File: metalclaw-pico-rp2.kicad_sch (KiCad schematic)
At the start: 123 parts, among them J1 USB4105-GF-A, J2 FTSH-105-01-L-DV-K, SW1 PTS810SJM250SMTR LFS, SW2 PTS810SJM250SMTR LFS, U1 XC6220B331MR-G, U2 RP2354B, U3 APS6404L-3SQR-SN, Y1 ABM8-272-T3

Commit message: Route USB, PSRAM and first quadrant signals
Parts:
- D1: value PMEG2010ER,115 -> CUHS20F30,H3F; footprint Diode_SMD:Nexperia_CFP3_SOD-123W -> Diode_SMD:D_SOD-323F; Mouser 771-PMEG2010ER115 -> 757-CUHS20F30H3F
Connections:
- net USB_D-: now reaches R80.2, U2.66 (USB_DM)
- net USB_D+: now reaches R81.2, U2.67 (USB_DP)
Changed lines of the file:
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@@
 		)
 	)
+	(label "USB_D+"
+		(at 330.2 123.19 180)
+		(effects
+			(font
+				(size 1.27 1.27)
+			)
+			(justify right bottom)
+		)
+	)
 	(label "GP7"
 		(at 43.18 172.72 0)
@@
 		)
 	)
+	(label "USB_D-"
+		(at 330.2 120.65 180)
+		(effects
+			(font
+				(size 1.27 1.27)
+			)
+			(justify right bottom)
+		)
+	)
 	(label "GP26"
 		(at 191.77 182.88 180)
@@
 			)
 		)
-		(property "Value" "PMEG2010ER,115"
+		(property "Value" "CUHS20F30,H3F"
 			(at 343.8525 69.85 0)
 			(effects
@@
 			)
 		)
-		(property "Footprint" "Diode_SMD:Nexperia_CFP3_SOD-123W"
+		(property "Footprint" "Diode_SMD:D_SOD-323F"
 			(at 344.17 73.66 0)
 			(effects
@@
 			)
 		)
-		(property "Datasheet" "https://assets.nexperia.com/documents/data-sheet/PMEG2010ER.pdf"
+		(property "Datasheet" "https://toshiba.semicon-storage.com/info/CUHS20F30_datasheet_en_20250926.pdf?did=63604&prodName=CUHS20F30"
 			(at 344.17 73.66 0)
 			(effects
@@
 			)
 		)
-		(property "Description" "20 V 1 A low-forward-voltage Schottky rectifier, SOD-123W, Nexperia PMEG2010ER,115"
+		(property "Description" "30 V 2 A Schottky barrier diode, SOD-323HE (US2H), Toshiba CUHS20F30,H3F"
 			(at 344.17 73.66 0)
 			(effects
@@
 			)
 		)
-		(property "Mouser" "771-PMEG2010ER115"
+		(property "Mouser" "757-CUHS20F30H3F"
 			(at 344.17 73.66 0)
 			(effects

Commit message: Route all signals
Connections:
- net USB_D+: now also J1.A6 (D+), J1.B6 (D+), R81.1; no longer R81.2, U2.67 (USB_DP)
- net USB_D-: now also J1.A7 (D-), J1.B7 (D-), R80.1; no longer R80.2, U2.66 (USB_DM)
- new net: R80.2, U2.66 (USB_DM)
- new net: R81.2, U2.67 (USB_DP)
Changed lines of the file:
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@@
 	)
 	(label "USB_D+"
-		(at 330.2 123.19 180)
+		(at 347.98 123.19 180)
 		(effects
 			(font
@@
 	)
 	(label "USB_D-"
-		(at 330.2 120.65 180)
-		(effects
-			(font
+		(at 347.98 120.65 180)
+		(effects
+			(font

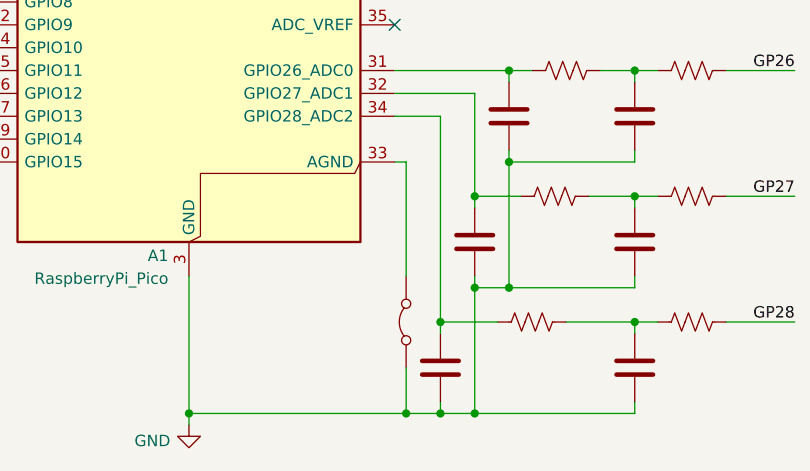
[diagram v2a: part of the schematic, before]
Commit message: Rearrange power passives
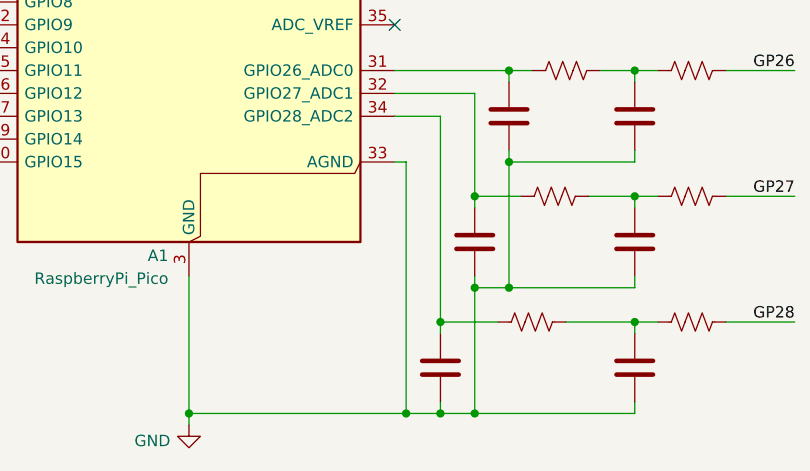
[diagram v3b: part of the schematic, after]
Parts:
- removed JP1: Jumper_2_Bridged, Jumper:SolderJumper-2_P1.3mm_Bridged2Bar_Pad1.0x1.5mm, symbol Jumper:Jumper_2_Bridged
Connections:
- net GND: now also A1.33 (AGND)
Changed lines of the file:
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@@
 	(wire
 		(pts
-			(xy 148.59 215.9) (xy 148.59 220.98)
+			(xy 148.59 193.04) (xy 148.59 220.98)
 		)
 		(stroke
@@
 	(wire
 		(pts
-			(xy 148.59 193.04) (xy 148.59 205.74)
-		)
-		(stroke
-			(width 0)
-			(type default)
-		)
-	)
-	(wire
-		(pts
 			(xy 257.81 105.41) (xy 245.11 105.41)
 		)
@@
 					(unit 1)
 				)
-			)
-		)
-	)
-	(symbol
-		(lib_id "Jumper:Jumper_2_Bridged")
-		(at 148.59 210.82 90)
-		(unit 1)
-		(exclude_from_sim no)
-		(in_bom no)
-		(on_board yes)
-		(dnp no)
-		(property "Reference" "JP1"
-			(at 146.05 209.5499 90)
-			(effects
-				(font
-					(size 1.27 1.27)
-				)
-				(justify left)
-				(hide yes)
-			)
-		)
-		(property "Value" "Jumper_2_Bridged"
-			(at 146.05 212.0899 90)
-			(effects
-				(font
-					(size 1.27 1.27)
-				)
-				(justify left)
-				(hide yes)
-			)
-		)
-		(property "Footprint" "Jumper:SolderJumper-2_P1.3mm_Bridged2Bar_Pad1.0x1.5mm"
-			(at 148.59 210.82 0)
-			(effects
-				(font
-					(size 1.27 1.27)
-				)
-				(hide yes)
-			)
-		)
-		(property "Datasheet" "~"
-			(at 148.59 210.82 0)
-			(effects
-				(font
-					(size 1.27 1.27)
-				)
-				(hide yes)
-			)
-		)
-		(property "Description" "Jumper, 2-pole, closed/bridged"
-			(at 148.59 210.82 0)
-			(effects
-				(font
-					(size 1.27 1.27)
-				)
-				(hide yes)
-			)
-		)
-		(property "KLC_S4.2_DVDD" ""
-			(at 148.59 210.82 90)
-			(effects
-				(font
-					(size 1.27 1.27)
-				)
-				(hide yes)
-			)
-		)
-		(property "KLC_S4.2_VREG_LX" ""
-			(at 148.59 210.82 90)
-			(effects
-				(font
-					(size 1.27 1.27)
-				)
-				(hide yes)
-			)
-		)
-		(pin "1"
-		)
-		(pin "2"
-		)
-		(instances
-			(project ""
-				(path "/c83ebc88-59c8-491c-acdb-d3cfac2d55f0"
-					(reference "JP1")
-					(unit 1)
-				)

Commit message: Castellate A1 edge pads, fix D1 footprint (US2H), GND stitching, DRC clean
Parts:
- D1: footprint Diode_SMD:D_SOD-323F -> MetalClaw:D_US2H_CUHS20F30
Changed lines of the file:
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@@
 			)
 		)
-		(property "Footprint" "Diode_SMD:D_SOD-323F"
+		(property "Footprint" "MetalClaw:D_US2H_CUHS20F30"
 			(at 344.17 73.66 0)
 			(effects

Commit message: BOM: R83 CE pull-up 10k->2.2k, LCSC part numbers, L1 entry fix
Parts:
- C1, C2: LCSC (none) -> C19702; LCSC MPN (none) -> CL10A106KP8NNNC
- C10, C12, C13, C24: LCSC (none) -> C326586; LCSC MPN (none) -> CC0402KRX5R6BB475
- C11, C28: LCSC (none) -> C52923; LCSC MPN (none) -> CL05A105KA5NQNC
- C14, C15, C16, C17, C18, C19, C20, C21, C22, C23, C25, C3: LCSC (none) -> C190183; LCSC MPN (none) -> CC0201KRX5R6BB104
- C26, C27: LCSC (none) -> C85891
- C4, C5, C6: LCSC (none) -> C668348
- C7, C8, C9: LCSC (none) -> C326875; LCSC MPN (none) -> CC0201KRX7R8BB103
- D1: LCSC (none) -> C5357828
- J1: LCSC (none) -> C3020560
- J2: LCSC (none) -> C5155080
- L1: LCSC (none) -> C42411119
- R1, R10, R11, R12, R13, R14, R15, R16, R17, R19, R2, R20, R21, R22, R25, R27, R28, R29, R3, R4, R5, R6, R7, R79, R8, R82, R9: LCSC (none) -> C274341
- R18, R34, R42, R78: LCSC (none) -> C138165
- R23, R24, R26: LCSC (none) -> C142018
- R30, R31, R32: LCSC (none) -> C274872
- R33, R35, R36, R37, R38, R39, R40, R41, R43, R44, R45, R46, R47, R48, R49, R50, R51, R52, R53, R54, R55, R56, R57, R58, R59, R60, R61, R62, R63, R64, R65, R66, R67, R68, R69, R70, R71, R72, R74, R75, R76, R77: LCSC (none) -> C77623
- R73: LCSC (none) -> C25105; LCSC MPN (none) -> 0402WGF330JTCE
- R80, R81: LCSC (none) -> C273268
- R83: value 10k -> 2.2k; LCSC (none) -> C142018; Mouser 603-RC0201FR-0710KL -> 603-RC0201FR-072K2L
- SW1, SW2: LCSC (none) -> C116501
- U1: LCSC (none) -> C86534
- U2: LCSC (none) -> C39843328
- U3: LCSC (none) -> C5333729
- Y1: LCSC (none) -> C20625731

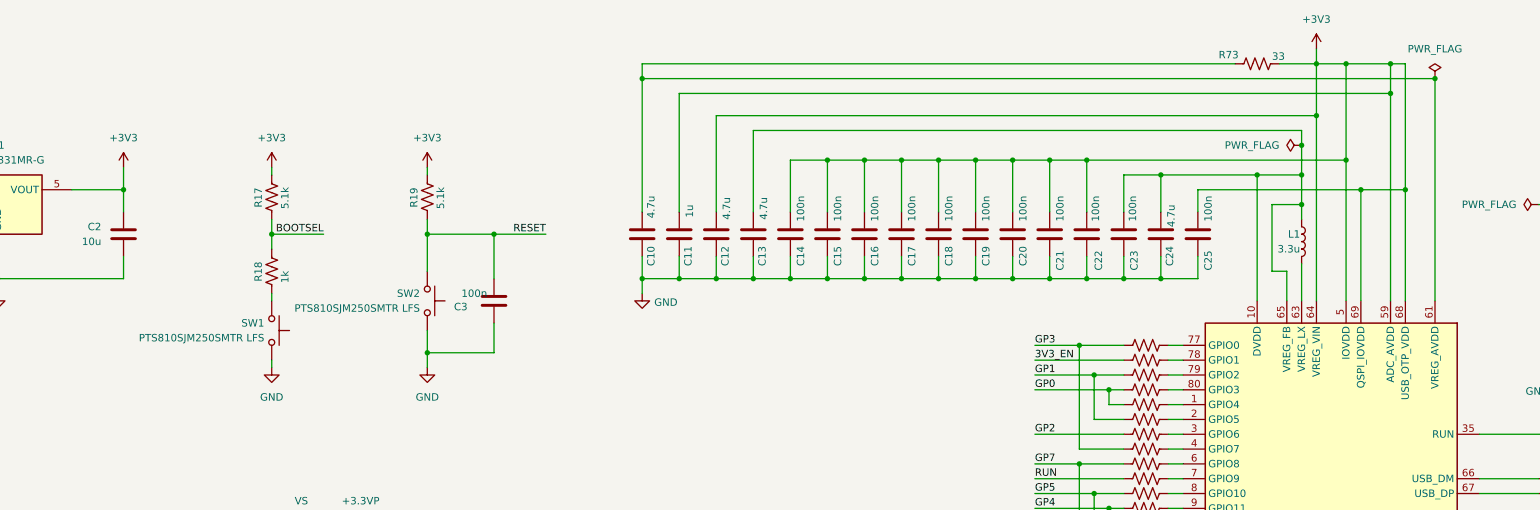
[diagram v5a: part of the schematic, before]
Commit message: Add decoupling for pin 51
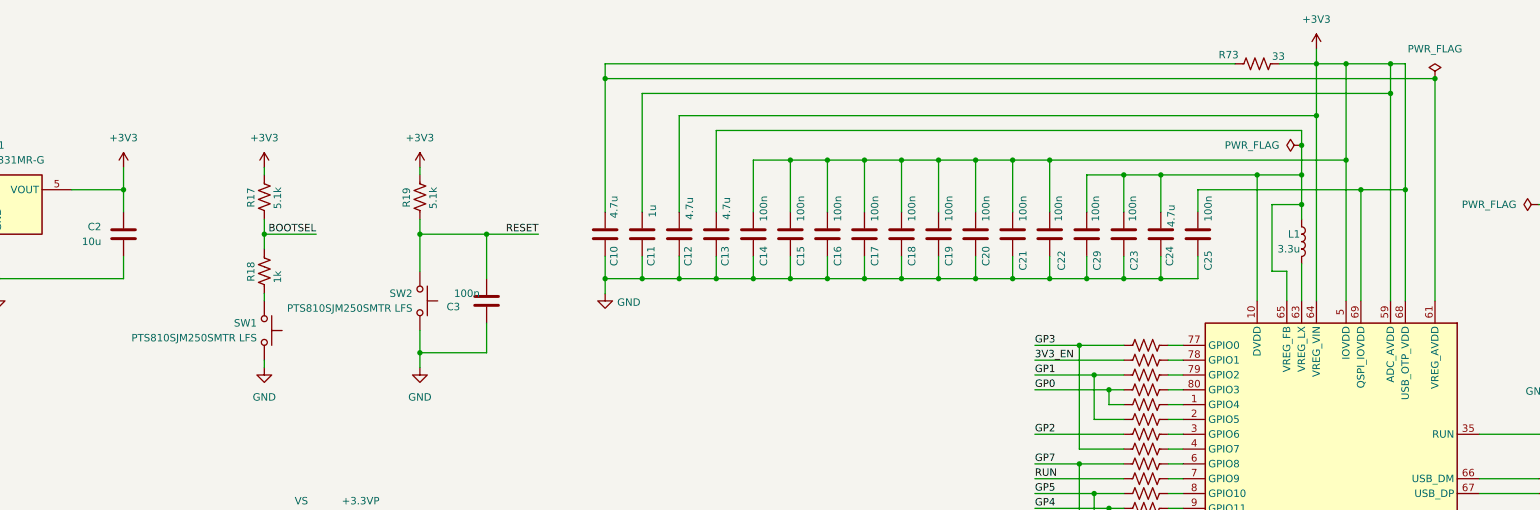
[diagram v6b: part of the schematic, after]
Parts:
- added C29: 100n, Capacitor_SMD:C_0201_0603Metric, symbol Device:C
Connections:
- net GND: now also C29.1
- net at C13.2, C23.2, C24.2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: now also C29.2
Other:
- moved on the sheet: C10, C11, C12, C13, C14, C15, C16, C17, C18, C19, C20, C21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

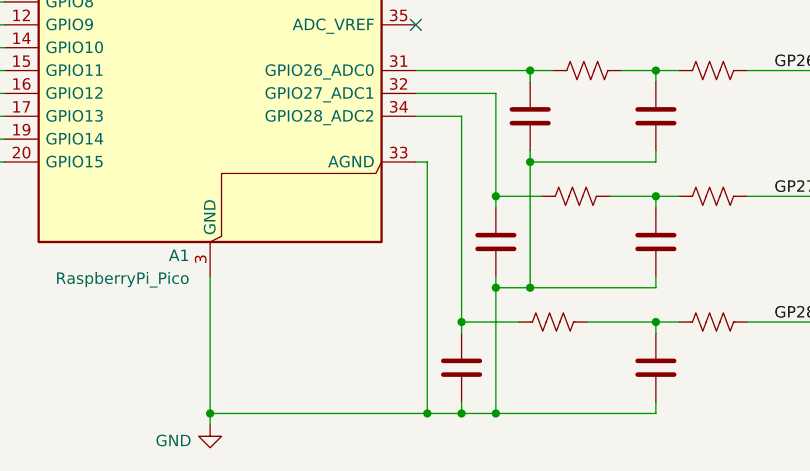
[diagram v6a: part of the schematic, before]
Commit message: Use net tie to connect AGND and GND
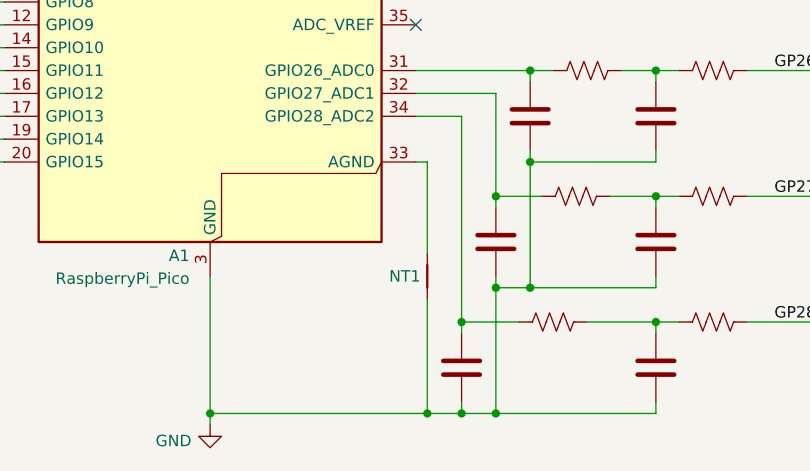
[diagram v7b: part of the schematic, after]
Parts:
- added NT1: NetTie_2, NetTie:NetTie-2_SMD_Pad0.5mm, symbol Device:NetTie_2
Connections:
- net GND: now also NT1.1; no longer A1.33 (AGND)
- new net: A1.33 (AGND), NT1.2
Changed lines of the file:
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@@
 	)
 	(junction
+		(at 148.59 220.98)
+		(diameter 0)
+		(color 0 0 0 0)
+	)
+	(junction
 		(at 171.45 86.36)
 		(diameter 0)
@@
 	)
 	(junction
-		(at 148.59 220.98)
-		(diameter 0)
-		(color 0 0 0 0)
-	)
-	(junction
 		(at 364.49 193.04)
 		(diameter 0)
@@
 	(wire
 		(pts
-			(xy 148.59 193.04) (xy 148.59 220.98)
-		)
-		(stroke
-			(width 0)
-			(type default)
-		)
-	)
-	(wire
-		(pts
 			(xy 124.46 220.98) (xy 124.46 222.25)
 		)
@@
 	(wire
 		(pts
+			(xy 148.59 208.28) (xy 148.59 220.98)
+		)
+		(stroke
+			(width 0)
+			(type default)
+		)
+	)
+	(wire
+		(pts
 			(xy 93.98 139.7) (xy 101.6 139.7)
 		)
@@
 	(wire
 		(pts
-			(xy 148.59 220.98) (xy 152.4 220.98)
-		)
-		(stroke
-			(width 0)
-			(type default)
-		)
-	)
-	(wire
-		(pts
 			(xy 254 86.36) (xy 247.65 86.36)
 		)
@@
 	(wire
 		(pts
+			(xy 148.59 220.98) (xy 152.4 220.98)
+		)
+		(stroke
+			(width 0)
+			(type default)
+		)
+	)
+	(wire
+		(pts
 			(xy 370.84 185.42) (xy 364.49 185.42)
 		)
@@
 	(wire
 		(pts
+			(xy 148.59 193.04) (xy 148.59 203.2)
+		)
+		(stroke
+			(width 0)
+			(type default)
+		)
+	)
+	(wire
+		(pts
 			(xy 43.18 170.18) (xy 62.23 170.18)
 		)
@@
 					(unit 1)
 				)
+			)
+		)
+	)
+	(symbol
+		(lib_id "Device:NetTie_2")
+		(at 148.59 205.74 90)
+		(unit 1)
+		(exclude_from_sim no)
+		(in_bom no)
+		(on_board yes)
+		(dnp no)
+		(property "Reference" "NT1"
+			(at 147.828 205.74 90)
+			(effects
+				(font
+					(size 1.27 1.27)
+				)
+				(justify left)
+			)
+		)
+		(property "Value" "NetTie_2"
+			(at 147.32 207.0099 90)
+			(effects
+				(font
+					(size 1.27 1.27)
+				)
+				(justify left)
+				(hide yes)
+			)
+		)
+		(property "Footprint" "NetTie:NetTie-2_SMD_Pad0.5mm"
+			(at 148.59 205.74 0)
+			(effects
+				(font
+					(size 1.27 1.27)
+				)
+				(hide yes)
+			)
+		)
+		(property "Datasheet" "~"
+			(at 148.59 205.74 0)
+			(effects
+				(font
+					(size 1.27 1.27)
+				)
+				(hide yes)
+			)
+		)
+		(property "Description" "Net tie, 2 pins"
+			(at 148.59 205.74 0)
+			(effects
+				(font
+					(size 1.27 1.27)
+				)
+				(hide yes)
+			)
+		)
+		(pin "1"
+		)
+		(pin "2"
+		)
+		(instances
+			(project ""
+				(path "/c83ebc88-59c8-491c-acdb-d3cfac2d55f0"
+					(reference "NT1")
+					(unit 1)
+				)

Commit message: Fix last warning and regen fab
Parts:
- J1: footprint Connector_USB:USB_C_Receptacle_GCT_USB4105-xx-A_16P_TopMnt_Horizontal -> MetalClaw:USB_C_Receptacle_GCT_USB4105-xx-A_16P_TopMnt_Horizontal
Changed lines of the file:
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@@
 			)
 		)
-		(property "Footprint" "Connector_USB:USB_C_Receptacle_GCT_USB4105-xx-A_16P_TopMnt_Horizontal"
+		(property "Footprint" "MetalClaw:USB_C_Receptacle_GCT_USB4105-xx-A_16P_TopMnt_Horizontal"
 			(at 367.03 88.9 0)
 			(effects
